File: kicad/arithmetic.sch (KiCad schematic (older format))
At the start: 68 parts, among them J1 Conn_01x03_Male, J2 Conn_01x05_Male, J3 Conn_01x05_Male, J4 Conn_Coaxial, J5 Conn_Coaxial, J6 Conn_Coaxial, U1 LM317, U2 LM337, U3 OPA197xDBV, U4 OPA197xDBV, U5 OPA197xDBV

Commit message: amended OPA197 for SOIC8 pin layout
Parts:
- removed U3, U4, U5: OPA197xDBV, Package_SO:SOIC-8_3.9x4.9mm_P1.27mm, symbol Amplifier_Operational:OPA197xDBV
- added U3, U4, U5: OPA197xD, Package_SO:SOIC-8_3.9x4.9mm_P1.27mm, symbol Amplifier_Operational:OPA197xD
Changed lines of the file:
@@
 Wire Wire Line
 	8600 2950 8750 2950
-$Comp
-L Amplifier_Operational:OPA197xDBV U4
-U 1 1 5E77CAA4
-P 9850 2450
-F 0 "U4" H 10150 2300 50  0000 C CNN
-F 1 "OPA197xDBV" H 10100 2200 50  0000 C CNN
-F 2 "Package_SO:SOIC-8_3.9x4.9mm_P1.27mm" H 9750 2250 50  0001 L CNN
-F 3 "http://www.ti.com/lit/ds/symlink/opa197.pdf" H 9850 2650 50  0001 C CNN
-	1    9850 2450
-	1    0    0    -1
-$EndComp
 Wire Wire Line
 	9400 3250 9400 2900
@@
 Wire Wire Line
 	5900 2750 6050 2750
-$Comp
-L Amplifier_Operational:OPA197xDBV U3
-U 1 1 5EAD1BE7
-P 7150 2450
-F 0 "U3" H 7450 2300 50  0000 C CNN
-F 1 "OPA197xDBV" H 7400 2200 50  0000 C CNN
-F 2 "Package_SO:SOIC-8_3.9x4.9mm_P1.27mm" H 7050 2250 50  0001 L CNN
-F 3 "http://www.ti.com/lit/ds/symlink/opa197.pdf" H 7150 2650 50  0001 C CNN
-	1    7150 2450
-	1    0    0    -1
-$EndComp
 Wire Wire Line
 	6700 3250 6700 3100
@@
 Wire Wire Line
 	5900 5500 6050 5500
-$Comp
-L Amplifier_Operational:OPA197xDBV U5
-U 1 1 5EE0464F
-P 7150 5200
-F 0 "U5" H 7450 5050 50  0000 C CNN
-F 1 "OPA197xDBV" H 7400 4950 50  0000 C CNN
-F 2 "Package_SO:SOIC-8_3.9x4.9mm_P1.27mm" H 7050 5000 50  0001 L CNN
-F 3 "http://www.ti.com/lit/ds/symlink/opa197.pdf" H 7150 5400 50  0001 C CNN
-	1    7150 5200
-	1    0    0    -1
-$EndComp
 Wire Wire Line
 	6700 6000 6700 5850
@@
 	6500 4700 6050 4700
 Connection ~ 6050 4700
+$Comp
+L Amplifier_Operational:OPA197xD U3
+U 1 1 5EA083BA
+P 7150 2450
+F 0 "U3" H 7300 2300 50  0000 L CNN
+F 1 "OPA197xD" H 7150 2200 50  0000 L CNN
+F 2 "Package_SO:SOIC-8_3.9x4.9mm_P1.27mm" H 7050 2250 50  0001 L CNN
+F 3 "http://www.ti.com/lit/ds/symlink/opa197.pdf" H 7300 2600 50  0001 C CNN
+	1    7150 2450
+	1    0    0    -1
+$EndComp
+$Comp
+L Amplifier_Operational:OPA197xD U5
+U 1 1 5EA0BE83
+P 9850 2450
+F 0 "U5" H 10000 2300 50  0000 L CNN
+F 1 "OPA197xD" H 9850 2200 50  0000 L CNN
+F 2 "Package_SO:SOIC-8_3.9x4.9mm_P1.27mm" H 9750 2250 50  0001 L CNN
+F 3 "http://www.ti.com/lit/ds/symlink/opa197.pdf" H 10000 2600 50  0001 C CNN
+	1    9850 2450
+	1    0    0    -1
+$EndComp
+$Comp
+L Amplifier_Operational:OPA197xD U4
+U 1 1 5EA0D7C6
+P 7150 5200
+F 0 "U4" H 7300 5050 50  0000 L CNN
+F 1 "OPA197xD" H 7150 4950 50  0000 L CNN
+F 2 "Package_SO:SOIC-8_3.9x4.9mm_P1.27mm" H 7050 5000 50  0001 L CNN
+F 3 "http://www.ti.com/lit/ds/symlink/opa197.pdf" H 7300 5350 50  0001 C CNN
+	1    7150 5200
+	1    0    0    -1
+$EndComp
 $EndSCHEMATC

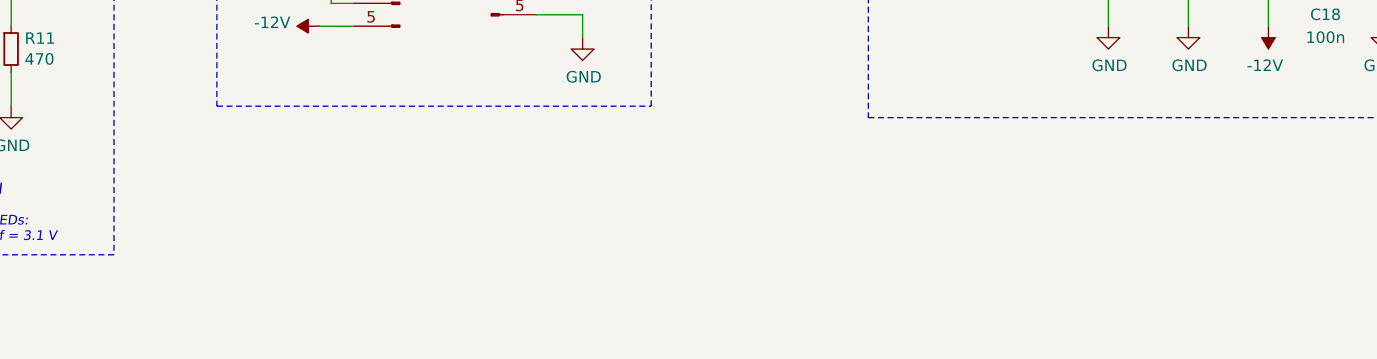
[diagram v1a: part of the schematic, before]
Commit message: added mounting holes to eeschema, replaced mounting holes with pad
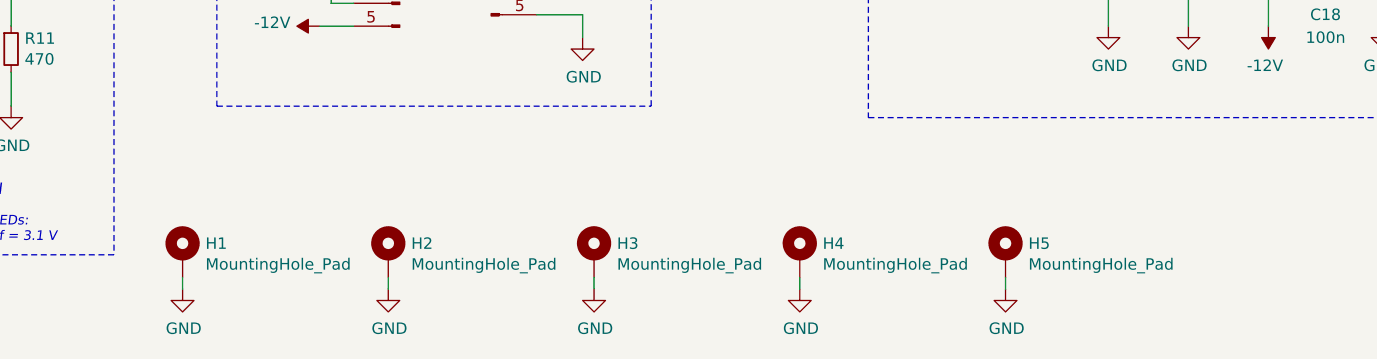
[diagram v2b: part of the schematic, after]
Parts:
- added H1, H2, H3, H4, H5: MountingHole_Pad, MountingHole:MountingHole_2.7mm_M2.5_Pad, symbol Mechanical:MountingHole_Pad
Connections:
- net GND: now also H1.1, H2.1, H3.1, H4.1, H5.1
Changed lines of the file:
@@
 	1    0    0    -1
 $EndComp
+$Comp
+L Mechanical:MountingHole_Pad H1
+U 1 1 5EACE9FB
+P 2300 7000
+F 0 "H1" H 2400 7049 50  0000 L CNN
+F 1 "MountingHole_Pad" H 2400 6958 50  0000 L CNN
+F 2 "MountingHole:MountingHole_2.7mm_M2.5_Pad" H 2300 7000 50  0001 C CNN
+F 3 "~" H 2300 7000 50  0001 C CNN
+	1    2300 7000
+	1    0    0    -1
+$EndComp
+$Comp
+L power:GND #PWR0113
+U 1 1 5EACEF0B
+P 2300 7150
+AR Path="/5EACEF0B" Ref="#PWR0113"  Part="1"
+AR Path="/5E4BE137/5EACEF0B" Ref="#PWR?"  Part="1"
+F 0 "#PWR0113" H 2300 6900 50  0001 C CNN
+F 1 "GND" H 2305 6977 50  0000 C CNN
+F 2 "" H 2300 7150 50  0001 C CNN
+F 3 "" H 2300 7150 50  0001 C CNN
+	1    2300 7150
+	1    0    0    -1
+$EndComp
+Wire Wire Line
+	2300 7150 2300 7100
+$Comp
+L Mechanical:MountingHole_Pad H2
+U 1 1 5EADD1F3
+P 3200 7000
+F 0 "H2" H 3300 7049 50  0000 L CNN
+F 1 "MountingHole_Pad" H 3300 6958 50  0000 L CNN
+F 2 "MountingHole:MountingHole_2.7mm_M2.5_Pad" H 3200 7000 50  0001 C CNN
+F 3 "~" H 3200 7000 50  0001 C CNN
+	1    3200 7000
+	1    0    0    -1
+$EndComp
+$Comp
+L power:GND #PWR0114
+U 1 1 5EADD1F9
+P 3200 7150
+AR Path="/5EADD1F9" Ref="#PWR0114"  Part="1"
+AR Path="/5E4BE137/5EADD1F9" Ref="#PWR?"  Part="1"
+F 0 "#PWR0114" H 3200 6900 50  0001 C CNN
+F 1 "GND" H 3205 6977 50  0000 C CNN
+F 2 "" H 3200 7150 50  0001 C CNN
+F 3 "" H 3200 7150 50  0001 C CNN
+	1    3200 7150
+	1    0    0    -1
+$EndComp
+Wire Wire Line
+	3200 7150 3200 7100
+$Comp
+L Mechanical:MountingHole_Pad H3
+U 1 1 5EAEAEF9
+P 4100 7000
+F 0 "H3" H 4200 7049 50  0000 L CNN
+F 1 "MountingHole_Pad" H 4200 6958 50  0000 L CNN
+F 2 "MountingHole:MountingHole_2.7mm_M2.5_Pad" H 4100 7000 50  0001 C CNN
+F 3 "~" H 4100 7000 50  0001 C CNN
+	1    4100 7000
+	1    0    0    -1
+$EndComp
+$Comp
+L power:GND #PWR0115
+U 1 1 5EAEAEFF
+P 4100 7150
+AR Path="/5EAEAEFF" Ref="#PWR0115"  Part="1"
+AR Path="/5E4BE137/5EAEAEFF" Ref="#PWR?"  Part="1"
+F 0 "#PWR0115" H 4100 6900 50  0001 C CNN
+F 1 "GND" H 4105 6977 50  0000 C CNN
+F 2 "" H 4100 7150 50  0001 C CNN
+F 3 "" H 4100 7150 50  0001 C CNN
+	1    4100 7150
+	1    0    0    -1
+$EndComp
+Wire Wire Line
+	4100 7150 4100 7100
+$Comp
+L Mechanical:MountingHole_Pad H4
+U 1 1 5EAF96D9
+P 5000 7000
+F 0 "H4" H 5100 7049 50  0000 L CNN
+F 1 "MountingHole_Pad" H 5100 6958 50  0000 L CNN
+F 2 "MountingHole:MountingHole_2.7mm_M2.5_Pad" H 5000 7000 50  0001 C CNN
+F 3 "~" H 5000 7000 50  0001 C CNN
+	1    5000 7000
+	1    0    0    -1
+$EndComp
+$Comp
+L power:GND #PWR0116
+U 1 1 5EAF96DF
+P 5000 7150
+AR Path="/5EAF96DF" Ref="#PWR0116"  Part="1"
+AR Path="/5E4BE137/5EAF96DF" Ref="#PWR?"  Part="1"
+F 0 "#PWR0116" H 5000 6900 50  0001 C CNN
+F 1 "GND" H 5005 6977 50  0000 C CNN
+F 2 "" H 5000 7150 50  0001 C CNN
+F 3 "" H 5000 7150 50  0001 C CNN
+	1    5000 7150
+	1    0    0    -1
+$EndComp
+Wire Wire Line
+	5000 7150 5000 7100
+$Comp
+L Mechanical:MountingHole_Pad H5
+U 1 1 5EB2DC32
+P 5900 7000
+F 0 "H5" H 6000 7049 50  0000 L CNN
+F 1 "MountingHole_Pad" H 6000 6958 50  0000 L CNN
+F 2 "MountingHole:MountingHole_2.7mm_M2.5_Pad" H 5900 7000 50  0001 C CNN
+F 3 "~" H 5900 7000 50  0001 C CNN
+	1    5900 7000
+	1    0    0    -1
+$EndComp
+$Comp
+L power:GND #PWR0117
+U 1 1 5EB2DC38
+P 5900 7150
+AR Path="/5EB2DC38" Ref="#PWR0117"  Part="1"
+AR Path="/5E4BE137/5EB2DC38" Ref="#PWR?"  Part="1"
+F 0 "#PWR0117" H 5900 6900 50  0001 C CNN
+F 1 "GND" H 5905 6977 50  0000 C CNN
+F 2 "" H 5900 7150 50  0001 C CNN
+F 3 "" H 5900 7150 50  0001 C CNN
+	1    5900 7150
+	1    0    0    -1
+$EndComp
+Wire Wire Line
+	5900 7150 5900 7100
 $EndSCHEMATC

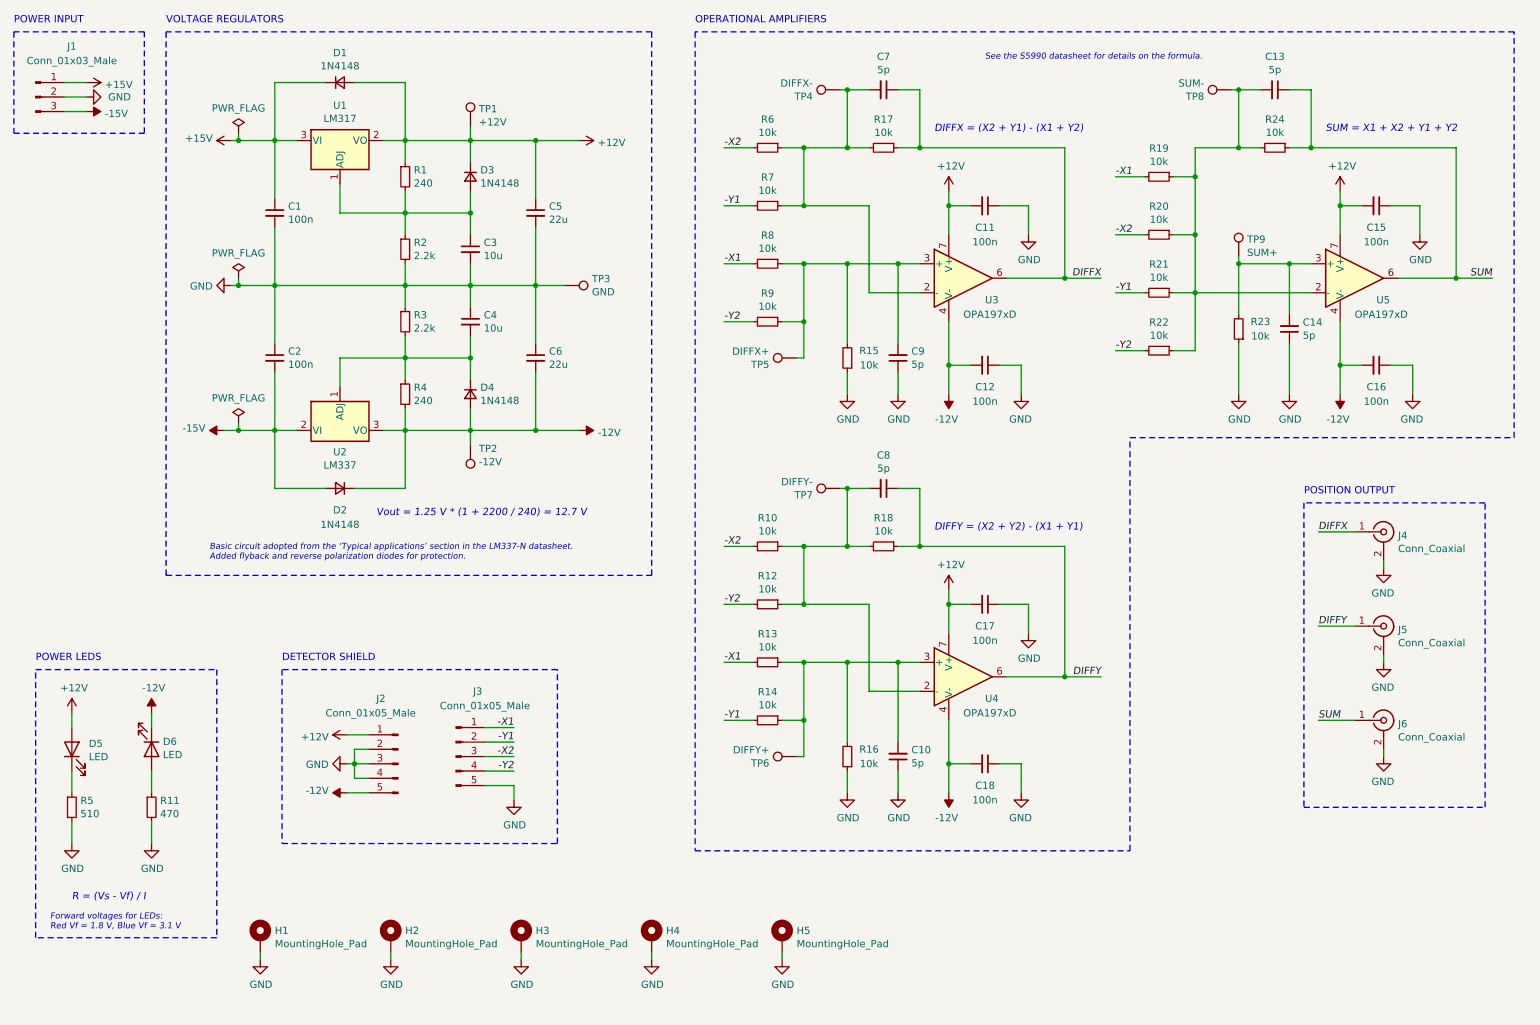
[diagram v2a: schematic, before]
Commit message: changed header shield pins for improved detector routing
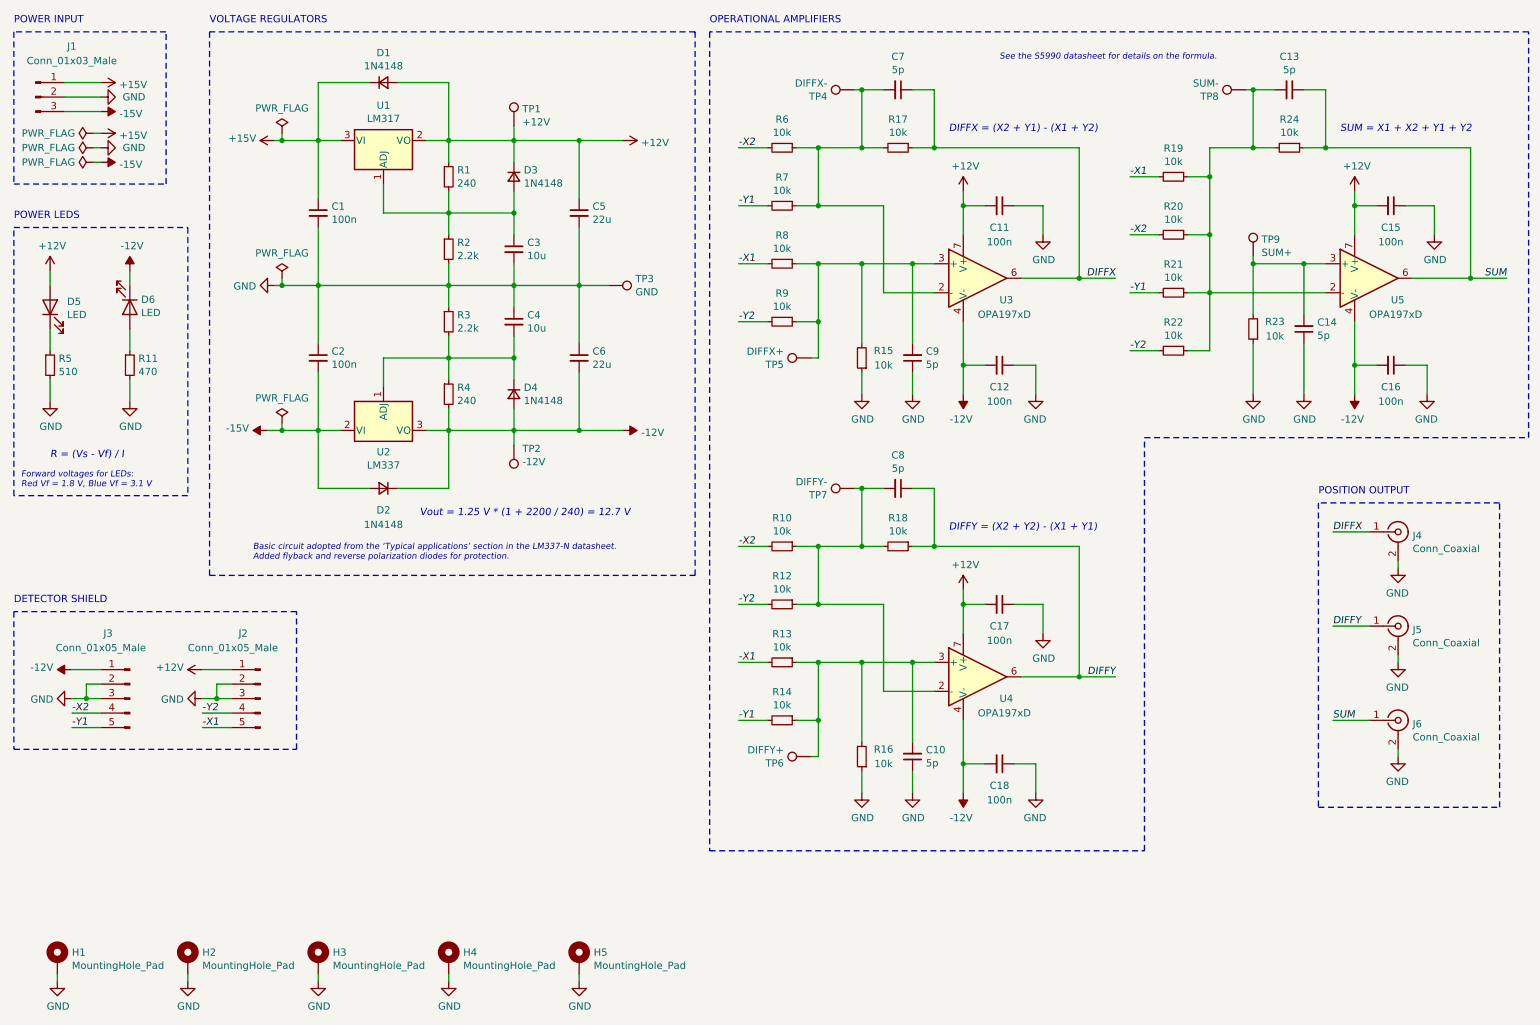
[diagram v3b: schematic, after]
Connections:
- net -12V: now also J3.1 (Pin_1); no longer J2.5 (Pin_5)
- net -X1: now also J2.5 (Pin_5); no longer J3.1 (Pin_1)
- net -X2: now also J3.4 (Pin_4); no longer J3.3 (Pin_3)
- net -Y1: now also J3.5 (Pin_5); no longer J3.2 (Pin_2)
- net -Y2: now also J2.4 (Pin_4); no longer J3.4 (Pin_4)
- net GND: now also J3.2 (Pin_2), J3.3 (Pin_3); no longer J2.4 (Pin_4), J3.5 (Pin_5)
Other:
- moved on the sheet: C1, C10, C11, C12, C13, C14, C15, C16, C17, C18, C2, C3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
